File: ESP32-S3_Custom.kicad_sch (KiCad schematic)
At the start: 1 part, among them U1 ESP32-S3-WROOM-1

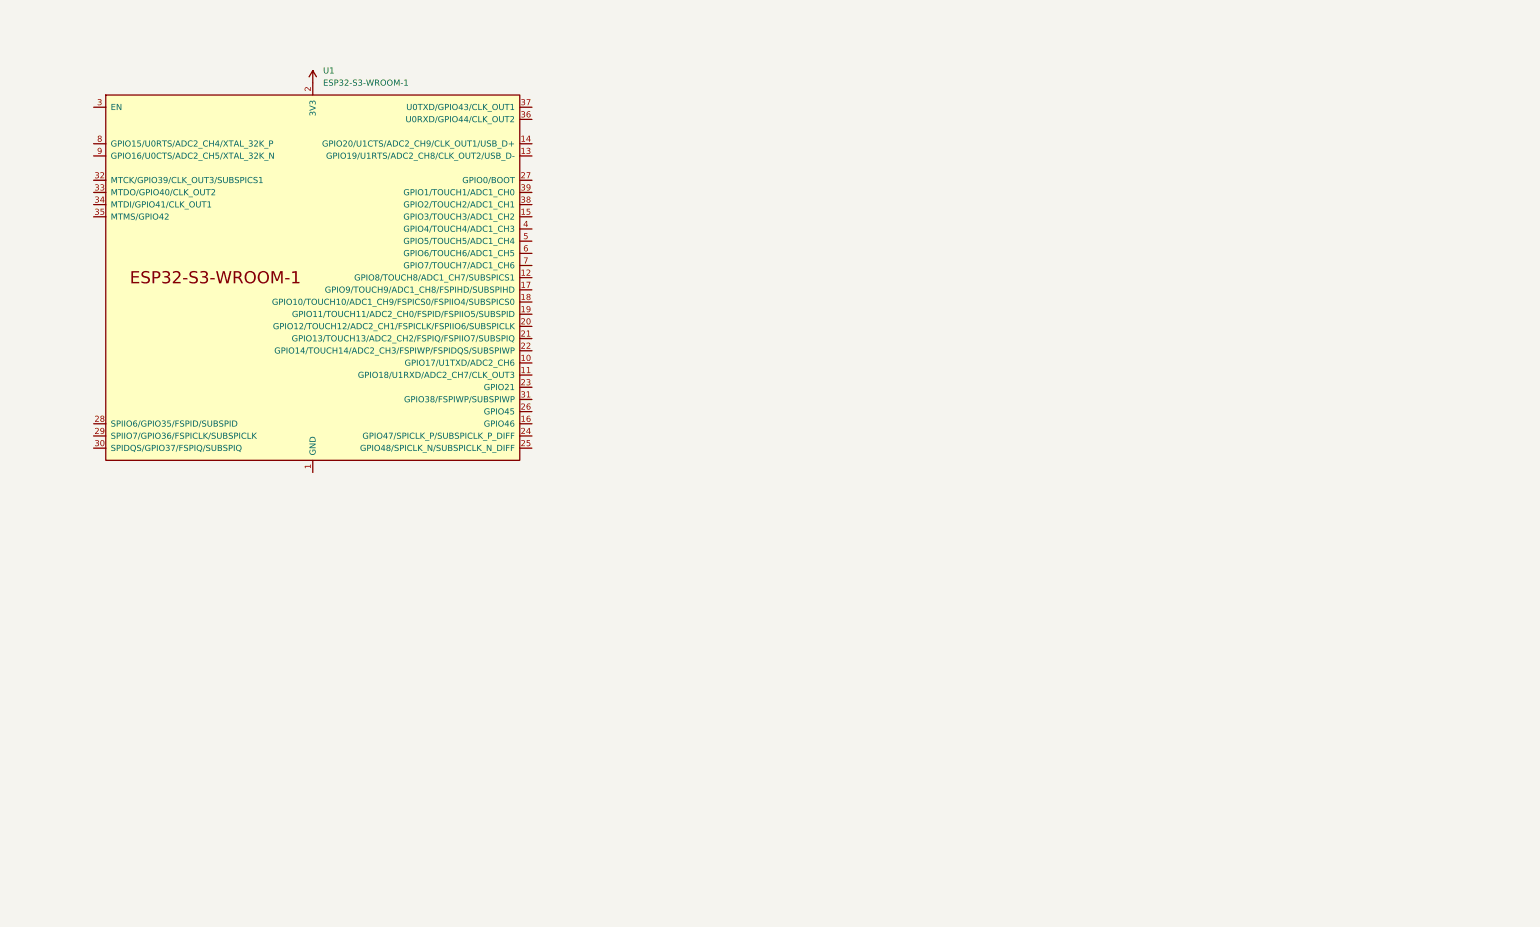
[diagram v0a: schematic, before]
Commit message: Added components
- USB-C connectors
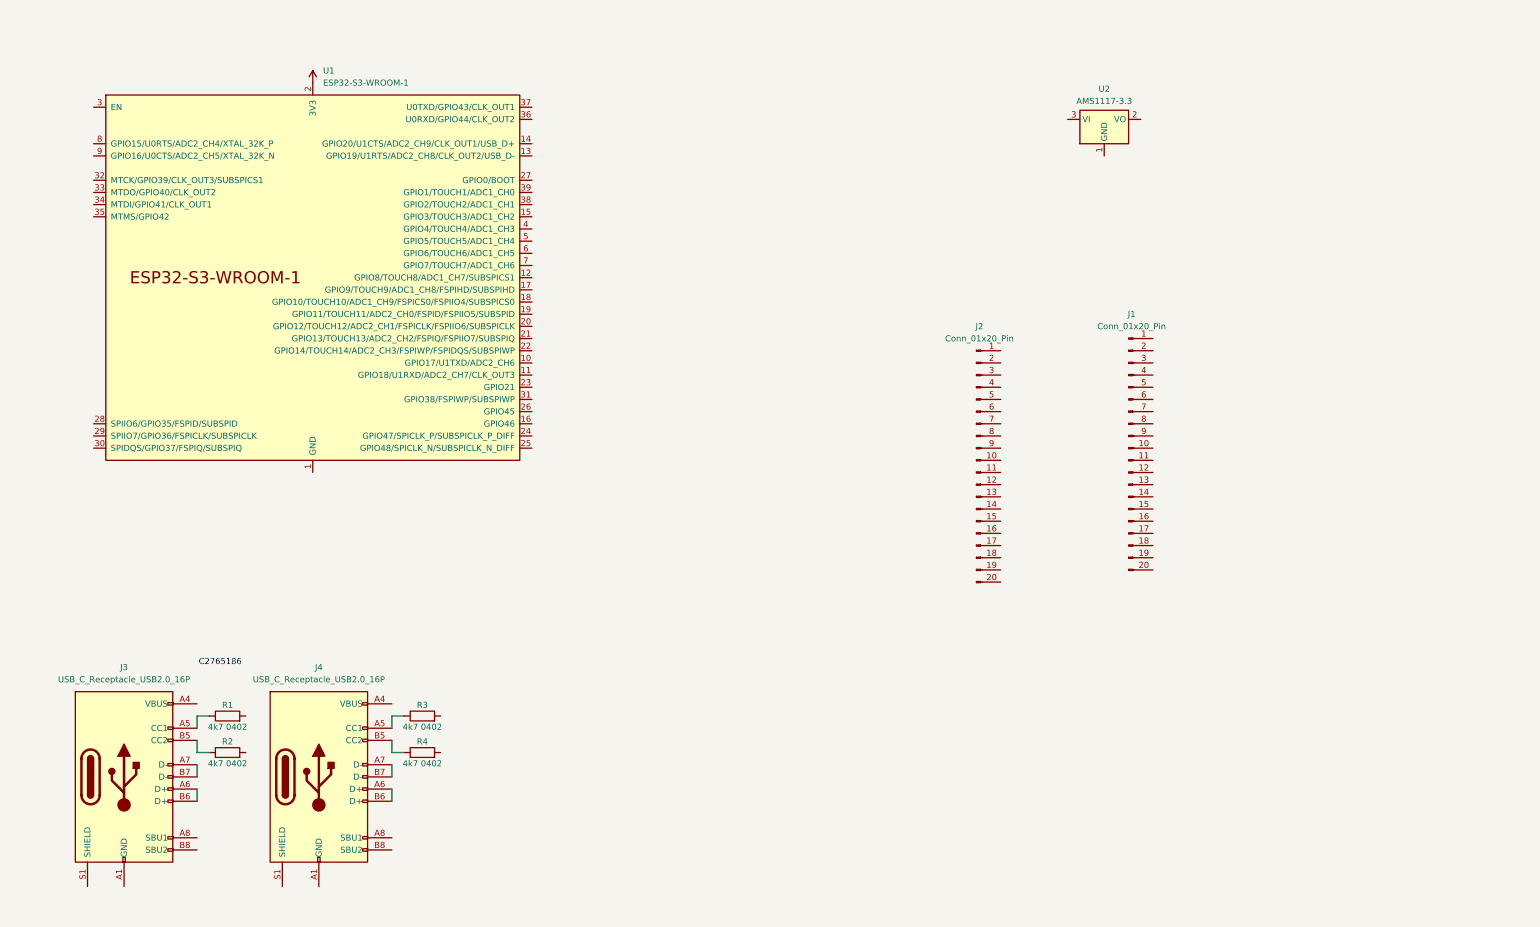
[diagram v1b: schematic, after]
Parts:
- added J1, J2: Conn_01x20_Pin, Connector_PinHeader_2.54mm:PinHeader_1x20_P2.54mm_Vertical, symbol Connector:Conn_01x20_Pin
- added J3, J4: USB_C_Receptacle_USB2.0_16P, Connector_USB:USB_C_Receptacle_G-Switch_GT-USB-7010ASV, symbol Connector:USB_C_Receptacle_USB2.0_16P
- added R1, R2, R3, R4: 4k7 0402, Resistor_SMD:R_0402_1005Metric, symbol Device:R
- added U2: AMS1117-3.3, Package_TO_SOT_SMD:SOT-223-3_TabPin2, symbol Regulator_Linear:AMS1117-3.3
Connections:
- new net: J4.B5 (CC2), R4.1
- new net: J3.A1 (GND), J3.A12 (GND), J3.B1 (GND), J3.B12 (GND)
- new net: J3.A4 (VBUS), J3.A9 (VBUS), J3.B4 (VBUS), J3.B9 (VBUS)
- new net: J3.A5 (CC1), R1.1
- new net: J3.A6 (D+), J3.B6 (D+)
- new net: J3.A7 (D-), J3.B7 (D-)
- new net: J3.B5 (CC2), R2.1
- new net: J4.A5 (CC1), R3.1
- new net: J4.A1 (GND), J4.A12 (GND), J4.B1 (GND), J4.B12 (GND)
- new net: J4.A4 (VBUS), J4.A9 (VBUS), J4.B4 (VBUS), J4.B9 (VBUS)
- new net: J4.A6 (D+), J4.B6 (D+)
- new net: J4.A7 (D-), J4.B7 (D-)
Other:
- note added: "C2765186"

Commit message: Added TF-01A component
- Added local library support.
  - linked component correctly.

NOTE: proj_foot was not the default for snap.

TODO: Ensure ESP32-S3 WROOM ports correctly
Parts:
- added MICRO_SD1: TF-01A, proj_foot:TF-01A, symbol uSD:TF-01A
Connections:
- new net SHIELD: MICRO_SD1.MP1 (SHIELD), MICRO_SD1.MP2 (SHIELD), MICRO_SD1.MP3 (SHIELD), MICRO_SD1.MP4 (SHIELD)
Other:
- note added: "C393941 C91145 - TF-01A"
- moved on the sheet: J1
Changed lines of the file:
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@@
+		)
+	)
+	(text "C393941\nC91145 - TF-01A"
+		(exclude_from_sim no)
+		(at 176.53 52.324 0)
+		(effects
+			(font
+				(size 1.27 1.27)
+			)
 		)
 	)
@@
 	(symbol
 		(lib_id "Connector:Conn_01x20_Pin")
-		(at 245.11 100.33 0)
+		(at 237.49 102.87 0)
 		(unit 1)
 		(exclude_from_sim no)
@@
 		(fields_autoplaced yes)
 		(property "Reference" "J1"
-			(at 245.745 72.39 0)
+			(at 238.125 74.93 0)
 			(effects
 				(font
@@
 		)
 		(property "Value" "Conn_01x20_Pin"
-			(at 245.745 74.93 0)
+			(at 238.125 77.47 0)
 			(effects
 				(font
@@
 		)
 		(property "Footprint" "Connector_PinHeader_2.54mm:PinHeader_1x20_P2.54mm_Vertical"
-			(at 245.11 100.33 0)
+			(at 237.49 102.87 0)
 			(effects
 				(font
@@
 		)
 		(property "Datasheet" "~"
-			(at 245.11 100.33 0)
+			(at 237.49 102.87 0)
 			(effects
 				(font
@@
 		)
 		(property "Description" "Generic connector, single row, 01x20, script generated"
-			(at 245.11 100.33 0)
+			(at 237.49 102.87 0)
 			(effects
 				(font
@@
 					(unit 1)
 				)
+			)
+		)
+	)
+	(symbol
+		(lib_id "uSD:TF-01A")
+		(at 176.53 38.1 0)
+		(unit 1)
+		(exclude_from_sim no)
+		(in_bom yes)
+		(on_board yes)
+		(dnp no)
+		(fields_autoplaced yes)
+		(property "Reference" "MICRO_SD1"
+			(at 176.53 22.86 0)
+			(effects
+				(font
+					(size 1.27 1.27)
+				)
+			)
+		)
+		(property "Value" "TF-01A"
+			(at 176.53 25.4 0)
+			(effects
+				(font
+					(size 1.27 1.27)
+				)
+			)
+		)
+		(property "Footprint" "proj_foot:TF-01A"
+			(at 176.53 38.1 0)
+			(effects
+				(font
+					(size 1.27 1.27)
+				)
+				(justify bottom)
+				(hide yes)
+			)
+		)
+		(property "Datasheet" ""
+			(at 176.53 38.1 0)
+			(effects
+				(font
+					(size 1.27 1.27)
+				)
+				(hide yes)
+			)
+		)
+		(property "Description" ""
+			(at 176.53 38.1 0)
+			(effects
+				(font
+					(size 1.27 1.27)
+				)
+				(hide yes)
+			)
+		)
+		(property "MF" "HRO Electronics Co., Ltd."
+			(at 176.53 38.1 0)
+			(effects
+				(font
+					(size 1.27 1.27)
+				)
+				(justify bottom)
+				(hide yes)
+			)
+		)
+		(property "Description_1" "Standard Card Edge Connectors"
+			(at 176.53 38.1 0)
+			(effects
+				(font
+					(size 1.27 1.27)
+				)
+				(justify bottom)
+				(hide yes)
+			)
+		)
+		(property "Package" "Package"
+			(at 176.53 38.1 0)
+			(effects
+				(font
+					(size 1.27 1.27)
+				)
+				(justify bottom)
+				(hide yes)
+			)
+		)
+		(property "Price" "None"
+			(at 176.53 38.1 0)
+			(effects
+				(font
+					(size 1.27 1.27)
+				)
+				(justify bottom)
+				(hide yes)
+			)
+		)
+		(property "SnapEDA_Link" "https://www.snapeda.com/parts/TF-01A/HRO+Electronics+Co.%252C+Ltd./view-part/?ref=snap"
+			(at 176.53 38.1 0)
+			(effects
+				(font
+					(size 1.27 1.27)
+				)
+				(justify bottom)
+				(hide yes)
+			)
+		)
+		(property "MP" "TF-01A"
+			(at 176.53 38.1 0)
+			(effects
+				(font
+					(size 1.27 1.27)
+				)
+				(justify bottom)
+				(hide yes)
+			)
+		)
+		(property "Availability" "Not in stock"
+			(at 176.53 38.1 0)
+			(effects
+				(font
+					(size 1.27 1.27)
+				)
+				(justify bottom)
+				(hide yes)
+			)
+		)
+		(property "Check_prices" "https://www.snapeda.com/parts/TF-01A/HRO+Electronics+Co.%252C+Ltd./view-part/?ref=eda"
+			(at 176.53 38.1 0)
+			(effects
+				(font
+					(size 1.27 1.27)
+				)
+				(justify bottom)
+				(hide yes)
+			)
+		)
+		(pin "5"
+		)
+		(pin "2"
+		)
+		(pin "8"
+		)
+		(pin "CD1"
+		)
+		(pin "MP1"
+		)
+		(pin "MP2"
+		)
+		(pin "7"
+		)
+		(pin "MP4"
+		)
+		(pin "4"
+		)
+		(pin "MP3"
+		)
+		(pin "3"
+		)
+		(pin "6"
+		)
+		(pin "1"
+		)
+		(instances
+			(project ""
+				(path "/c58fd478-d1c5-4f16-91d9-be14adece428"
+					(reference "MICRO_SD1")
+					(unit 1)
+				)

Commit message: Adjusted 3D model for USB-C connectors
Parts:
- J3, J4: footprint Connector_USB:USB_C_Receptacle_G-Switch_GT-USB-7010ASV -> Connector_USB:USB_C_Receptacle_GCT_USB4105-xx-A_16P_TopMnt_Horizontal

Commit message: Shuffled some parts around
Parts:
- added U3: CH340K, Package_SO:SSOP-10-1EP_3.9x4.9mm_P1mm_EP2.1x3.3mm, symbol Interface_USB:CH340K
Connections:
- new net: U3.11 (GND), U3.3 (GND)
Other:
- note added: "6Mbps - C2846043 2Mbps - C968586"
- note added: "C5129967"
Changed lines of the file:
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@@
 	(generator_version "9.0")
 	(paper "A4")
+	(text "C5129967"
+		(exclude_from_sim no)
+		(at 168.402 105.156 0)
+		(effects
+			(font
+				(size 1.27 1.27)
+			)
+		)
+	)
+	(text "6Mbps - C2846043\n2Mbps - C968586"
+		(exclude_from_sim no)
+		(at 145.288 146.304 0)
+		(effects
+			(font
+				(size 1.27 1.27)
+			)
+		)
+	)
 	(text "C2765186"
 		(exclude_from_sim no)
@@
 					(unit 1)
 				)
+			)
+		)
+	)
+	(symbol
+		(lib_id "Interface_USB:CH340K")
+		(at 144.78 171.45 0)
+		(unit 1)
+		(exclude_from_sim no)
+		(in_bom yes)
+		(on_board yes)
+		(dnp no)
+		(fields_autoplaced yes)
+		(property "Reference" "U3"
+			(at 146.9233 186.69 0)
+			(effects
+				(font
+					(size 1.27 1.27)
+				)
+				(justify left)
+			)
+		)
+		(property "Value" "CH340K"
+			(at 146.9233 189.23 0)
+			(effects
+				(font
+					(size 1.27 1.27)
+				)
+				(justify left)
+			)
+		)
+		(property "Footprint" "Package_SO:SSOP-10-1EP_3.9x4.9mm_P1mm_EP2.1x3.3mm"
+			(at 146.05 185.42 0)
+			(effects
+				(font
+					(size 1.27 1.27)
+				)
+				(justify left)
+				(hide yes)
+			)
+		)
+		(property "Datasheet" "https://cdn.sparkfun.com/assets/5/0/a/8/5/CH340DS1.PDF"
+			(at 135.89 151.13 0)
+			(effects
+				(font
+					(size 1.27 1.27)
+				)
+				(hide yes)
+			)
+		)
+		(property "Description" "USB serial converter, UART, SSOP-10"
+			(at 144.78 171.45 0)
+			(effects
+				(font
+					(size 1.27 1.27)
+				)
+				(hide yes)
+			)
+		)
+		(pin "11"
+		)
+		(pin "7"
+		)
+		(pin "2"
+		)
+		(pin "1"
+		)
+		(pin "10"
+		)
+		(pin "3"
+		)
+		(pin "8"
+		)
+		(pin "9"
+		)
+		(pin "5"
+		)
+		(pin "4"
+		)
+		(pin "6"
+		)
+		(instances
+			(project ""
+				(path "/c58fd478-d1c5-4f16-91d9-be14adece428"
+					(reference "U3")
+					(unit 1)
+				)

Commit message: any msg
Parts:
- added C14: 1uf, symbol Device:C
- added D1: RED, symbol Device:LED
- added D2: BLUE, symbol Device:LED
- added D3: GREEN, symbol Device:LED
- added R10, R11, R12, R13: 5.1k, symbol Device:R
- added SW1, SW2: SW_Push, symbol Switch:SW_Push
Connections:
- net +3.3V: now also R10.1, R13.2
- new net: D2.2 (A), R11.2
- new net: D3.2 (A), R12.2
- new net: D1.2 (A), R10.2
- new net +5V: R11.1
- new net GND: C14.2, D1.1 (K), D2.1 (K), D3.1 (K), SW1.2, SW2.1
- new net en: C14.1, R13.1, SW2.2
- new net gpio0: SW1.1
- new net gpio21: R12.1

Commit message: semidone
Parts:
- removed C14: 1uf, symbol Device:C
- removed D3: GREEN, symbol Device:LED
- removed SW1, SW2: SW_Push, symbol Switch:SW_Push
- added C1, C6: 1.2nf, symbol Device:C
- added C11, C4, C7, C8: 0.1uf, symbol Device:C
- added C2: 100nf, symbol Device:C
- added C3, C9: 10uf, symbol Device:C
- added C5: 22uf, symbol Device:C
- added D3: SK6812MINI, LED_SMD:LED_SK6812MINI_PLCC4_3.5x3.5mm_P1.75mm, symbol LED:SK6812MINI
- added Q1, Q2: S8050, Package_TO_SOT_THT:TO-92_Inline, symbol Transistor_BJT:S8050
- added R5, R6: 1M, symbol Device:R
- added R7, R8: 10k, symbol Device:R
- added R9: 4.7k, symbol Device:R
- added U4: LD1117S33TR_SOT223, Package_TO_SOT_SMD:SOT-223-3_TabPin2, symbol Regulator_Linear:LD1117S33TR_SOT223
- R12, R13: value 5.1k -> 4.7k
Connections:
- net SHIELD is gone; now on net GND: MICRO_SD1.MP1 (SHIELD), MICRO_SD1.MP2 (SHIELD), MICRO_SD1.MP3 (SHIELD), MICRO_SD1.MP4 (SHIELD)
- net en is gone; now on net +3.3V: R13.1
- net gpio21 is gone; now on net +3.3V: R12.1
- net +3.3V: now also MICRO_SD1.4 (VDD), U1.19 (GPIO11/TOUCH11/ADC2_CH0/FSPID/FSPIIO5/SUBSPID), C3.1, C4.1, C5.1, C8.1, C9.1, D3.4 (VDD), R9.1, U4.2 (VO); no longer R13.2
- net +5V: now also J3.A4 (VBUS), J3.A9 (VBUS), J3.B4 (VBUS), J3.B9 (VBUS), J4.A4 (VBUS), J4.A9 (VBUS), J4.B4 (VBUS), J4.B9 (VBUS), U3.7 (VCC), C2.1, C7.2, U4.3 (VI)
- net GND: now also J3.A1 (GND), J3.A12 (GND), J3.B1 (GND), J3.B12 (GND), J4.A1 (GND), J4.A12 (GND), J4.B1 (GND), J4.B12 (GND), MICRO_SD1.6 (VSS), R1.2, R2.2, R3.2, R4.2, U1.1 (GND), U1.40 (GND), U1.41 (GND), U3.11 (GND), U3.3 (GND), C1.2, C11.1, C2.2, C3.2, C4.2, C5.2, C6.2, C7.1, C8.2, C9.2, D3.2 (VSS), R5.2, R6.2, U4.1 (GND)
- net at R12.2: now also MICRO_SD1.7 (DAT0)
- net -D: now reaches U1.13 (GPIO19/U1RTS/ADC2_CH8/CLK_OUT2/USB_D-)
- net -D: now also J3.A7 (D-), J3.B7 (D-)
- net +D: now reaches U1.14 (GPIO20/U1CTS/ADC2_CH9/CLK_OUT1/USB_D+)
- net +D: now also J3.A6 (D+), J3.B6 (D+)
- net GPIO10: now reaches U1.18 (GPIO10/TOUCH10/ADC1_CH9/FSPICS0/FSPIIO4/SUBSPICS0)
- net GPIO10: now also MICRO_SD1.3 (CMD), R9.2
- net GPIO12: now reaches U1.20 (GPIO12/TOUCH12/ADC2_CH1/FSPICLK/FSPIIO6/SUBSPICLK)
- net GPIO12: now also MICRO_SD1.5 (CLK)
- net GPIO13: now reaches U1.21 (GPIO13/TOUCH13/ADC2_CH2/FSPIQ/FSPIIO7/SUBSPIQ)
- net GPIO13: now also MICRO_SD1.2 (CD/DAT3), R13.2
- net GPIO21: now reaches U1.23 (GPIO21)
- net GPIO21: now also D3.3 (DIN)
- net RX: now reaches U1.36 (U0RXD/GPIO44/CLK_OUT2)
- net RX: now also U3.8 (TXD)
- net TX: now reaches U1.37 (U0TXD/GPIO43/CLK_OUT1)
- net TX: now also U3.9 (RXD)
- net at U3.1 (UD+): now also J4.A6 (D+), J4.B6 (D+)
- net at U3.10 (V3): now also C11.2
- net at U3.2 (UD-): now also J4.A7 (D-), J4.B7 (D-)
- net at U3.4 (~{DTR}): now also Q2.1 (E), R7.2
- net at U3.6 (~{RTS}): now also Q1.1 (E), R8.1
- net at J3.S1 (SHIELD): now also C1.1, R5.1
- net at J4.S1 (SHIELD): now also C6.1, R6.1
- new net: Q1.2 (B), R7.1
- new net: Q2.2 (B), R8.2
- new net EN: Q1.3 (C)
- new net GPIO0: Q2.3 (C)
- no-connect marks 0 -> 2
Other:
- moved on the sheet: D1, D2, J1, J2, J3, J4, R1, R10, R11, R2, R3, R4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

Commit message: imu update
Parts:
- removed U2: AMS1117-3.3, Package_TO_SOT_SMD:SOT-223-3_TabPin2, symbol Regulator_Linear:AMS1117-3.3
- added J6: Conn_01x26, symbol Connector_Generic:Conn_01x26
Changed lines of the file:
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@@
-	)
-	(symbol
-		(lib_id "Regulator_Linear:AMS1117-3.3")
-		(at 321.31 16.51 0)
-		(unit 1)
-		(exclude_from_sim no)
-		(in_bom yes)
-		(on_board yes)
-		(dnp no)
-		(fields_autoplaced yes)
-		(property "Reference" "U2"
-			(at 321.31 10.16 0)
-			(effects
-				(font
-					(size 1.27 1.27)
-				)
-			)
-		)
-		(property "Value" "AMS1117-3.3"
-			(at 321.31 12.7 0)
-			(effects
-				(font
-					(size 1.27 1.27)
-				)
-			)
-		)
-		(property "Footprint" "Package_TO_SOT_SMD:SOT-223-3_TabPin2"
-			(at 321.31 11.43 0)
-			(effects
-				(font
-					(size 1.27 1.27)
-				)
-				(hide yes)
-			)
-		)
-		(property "Datasheet" "http://www.advanced-monolithic.com/pdf/ds1117.pdf"
-			(at 323.85 22.86 0)
-			(effects
-				(font
-					(size 1.27 1.27)
-				)
-				(hide yes)
-			)
-		)
-		(property "Description" "1A Low Dropout regulator, positive, 3.3V fixed output, SOT-223"
-			(at 321.31 16.51 0)
-			(effects
-				(font
-					(size 1.27 1.27)
-				)
-				(hide yes)
-			)
-		)
-		(pin "1"
-		)
-		(pin "2"
-		)
-		(pin "3"
-		)
-		(instances
-			(project ""
-				(path "/c58fd478-d1c5-4f16-91d9-be14adece428"
-					(reference "U2")
-					(unit 1)
-				)
-			)
-		)
 	)
 	(symbol
@@
 					(unit 1)
 				)
+			)
+		)
+	)
+	(symbol
+		(lib_id "Connector_Generic:Conn_01x26")
+		(at 179.07 87.63 90)
+		(unit 1)
+		(exclude_from_sim no)
+		(in_bom yes)
+		(on_board yes)
+		(dnp no)
+		(fields_autoplaced yes)
+		(property "Reference" "J6"
+			(at 180.34 81.28 90)
+			(effects
+				(font
+					(size 1.27 1.27)
+				)
+			)
+		)
+		(property "Value" "Conn_01x26"
+			(at 180.34 83.82 90)
+			(effects
+				(font
+					(size 1.27 1.27)
+				)
+			)
+		)
+		(property "Footprint" ""
+			(at 179.07 87.63 0)
+			(effects
+				(font
+					(size 1.27 1.27)
+				)
+				(hide yes)
+			)
+		)
+		(property "Datasheet" "~"
+			(at 179.07 87.63 0)
+			(effects
+				(font
+					(size 1.27 1.27)
+				)
+				(hide yes)
+			)
+		)
+		(property "Description" "Generic connector, single row, 01x26, script generated (kicad-library-utils/schlib/autogen/connector/)"
+			(at 179.07 87.63 0)
+			(effects
+				(font
+					(size 1.27 1.27)
+				)
+				(hide yes)
+			)
+		)
+		(pin "7"
+		)
+		(pin "4"
+		)
+		(pin "2"
+		)
+		(pin "3"
+		)
+		(pin "1"
+		)
+		(pin "5"
+		)
+		(pin "6"
+		)
+		(pin "9"
+		)
+		(pin "8"
+		)
+		(pin "13"
+		)
+		(pin "14"
+		)
+		(pin "10"
+		)
+		(pin "15"
+		)
+		(pin "11"
+		)
+		(pin "12"
+		)
+		(pin "22"
+		)
+		(pin "19"
+		)
+		(pin "24"
+		)
+		(pin "21"
+		)
+		(pin "23"
+		)
+		(pin "25"
+		)
+		(pin "26"
+		)
+		(pin "20"
+		)
+		(pin "18"
+		)
+		(pin "17"
+		)
+		(pin "16"
+		)
+		(instances
+			(project ""
+				(path "/c58fd478-d1c5-4f16-91d9-be14adece428"
+					(reference "J6")
+					(unit 1)
+				)
